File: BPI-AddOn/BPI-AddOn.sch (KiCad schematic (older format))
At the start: 61 parts, among them CON1 BARREL_JACK, J1 RJ45, J2 RJ45, J3 RJ45, P1 DIN10-1, P10 CONN_01X03, P11 CONN_01X05, P12 CONN_01X05, P13 CONN_01X08, P15 CONN_02X11, P16 USB_B, P17 CONN_01X05, P18 CONN_01X05, P19 V, P2 DIN10-2, P20 - +, P21 USB_OTG, P22 CONN_01X06, P23 CONN_01X06, P24 CONN_02X02, P25 CONN_01X02, P3 DIN10-3, P4 DIN10-4, P5 DIN10-5, P6 DIN7-1, P7 DIN7-2, P8 DIN7-3, P9 CONN_01X03, U1 MC34063, U2 FT230XS

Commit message: routing ...
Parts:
- R3: footprint w_pth_resistors:RC03 -> w_pth_resistors:RC05
- renumbered F3 to Fe1
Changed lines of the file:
@@
 $EndComp
 $Comp
-L R F3
+L R Fe1
 U 1 1 576471B3
 P 7450 4400
-F 0 "F3" V 7530 4400 50  0000 C CNN
+F 0 "Fe1" V 7530 4400 50  0000 C CNN
 F 1 "Ferrit" V 7450 4400 50  0000 C CNN
 F 2 "Resistors_SMD:R_0805_HandSoldering" V 7380 4400 50  0001 C CNN
@@
 F 0 "R3" V 2280 4450 50  0000 C CNN
 F 1 "120" V 2200 4450 50  0000 C CNN
-F 2 "w_pth_resistors:RC03" V 2130 4450 50  0001 C CNN
+F 2 "w_pth_resistors:RC05" V 2130 4450 50  0001 C CNN
 F 3 "" H 2200 4450 50  0000 C CNN
 	1    2200 4450

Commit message: wip
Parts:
- C5: value 10nF -> 100nF
- C8: value 10nF -> 4.7uF
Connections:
- wire segments 308 -> 305
- no-connect marks 23 -> 28
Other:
- moved on the sheet: C5, C9, CON1
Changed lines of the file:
@@
 	3700 5750 3800 5650
 Entry Wire Line
-	3800 5750 3900 5650
-Entry Wire Line
 	3900 5750 4000 5650
 Entry Wire Line
-	4000 5750 4100 5650
-Entry Wire Line
 	4100 5750 4200 5650
 Entry Wire Line
@@
 	4750 5750 4850 5650
 Entry Wire Line
-	4850 5750 4950 5650
-Entry Wire Line
 	4950 5750 5050 5650
-Entry Wire Line
-	5050 5750 5150 5650
 Entry Wire Line
 	5150 5750 5250 5650
@@
 CANL
 Text Label 4000 5550 1    60   ~ 0
-GND
-Text Label 3900 5550 1    60   ~ 0
-GND
-Text Label 4950 5550 1    60   ~ 0
 GND
 Text Label 5050 5550 1    60   ~ 0
@@
 Text Label 4750 5550 1    60   ~ 0
 GSB
-Text Label 4100 5550 1    60   ~ 0
-J1_V
 Text Label 4200 5550 1    60   ~ 0
 J1_V
-Text Label 5150 5550 1    60   ~ 0
-J2_V
 Text Label 5250 5550 1    60   ~ 0
 J2_V
@@
 L BARREL_JACK CON1
 U 1 1 575B93EA
-P 1550 6400
-F 0 "CON1" H 1550 6650 50  0000 C CNN
-F 1 "BARREL_JACK" H 1550 6200 50  0000 C CNN
-F 2 "w_conn_misc:dc_socket" H 1550 6400 50  0001 C CNN
-F 3 "" H 1550 6400 50  0000 C CNN
-	1    1550 6400
+P 1550 6450
+F 0 "CON1" H 1550 6700 50  0000 C CNN
+F 1 "BARREL_JACK" H 1550 6250 50  0000 C CNN
+F 2 "w_conn_misc:dc_socket" H 1550 6450 50  0001 C CNN
+F 3 "" H 1550 6450 50  0000 C CNN
+	1    1550 6450
 	1    0    0    -1
 $EndComp
@@
 L GNDA #PWR011
 U 1 1 575B9523
-P 2100 6600
-F 0 "#PWR011" H 2100 6350 50  0001 C CNN
-F 1 "GNDA" H 2100 6450 50  0000 C CNN
-F 2 "" H 2100 6600 50  0000 C CNN
-F 3 "" H 2100 6600 50  0000 C CNN
-	1    2100 6600
+P 2100 6650
+F 0 "#PWR011" H 2100 6400 50  0001 C CNN
+F 1 "GNDA" H 2100 6500 50  0000 C CNN
+F 2 "" H 2100 6650 50  0000 C CNN
+F 3 "" H 2100 6650 50  0000 C CNN
+	1    2100 6650
 	1    0    0    -1
 $EndComp
@@
 L C C9
 U 1 1 57645485
-P 8000 5900
-F 0 "C9" H 8025 6000 50  0000 L CNN
-F 1 "100nF" H 8025 5800 50  0000 L CNN
-F 2 "Resistors_SMD:R_0805_HandSoldering" H 8038 5750 50  0001 C CNN
-F 3 "" H 8000 5900 50  0000 C CNN
-	1    8000 5900
+P 7300 4750
+F 0 "C9" H 7325 4850 50  0000 L CNN
+F 1 "100nF" H 7325 4650 50  0000 L CNN
+F 2 "Resistors_SMD:R_0805_HandSoldering" H 7338 4600 50  0001 C CNN
+F 3 "" H 7300 4750 50  0000 C CNN
+	1    7300 4750
 	1    0    0    -1
 $EndComp
@@
 L C C5
 U 1 1 57653A31
-P 7300 4750
-F 0 "C5" H 7325 4850 50  0000 L CNN
-F 1 "10nF" H 7325 4650 50  0000 L CNN
-F 2 "Resistors_SMD:R_0805_HandSoldering" H 7338 4600 50  0001 C CNN
-F 3 "" H 7300 4750 50  0000 C CNN
-	1    7300 4750
+P 8000 5900
+F 0 "C5" H 8025 6000 50  0000 L CNN
+F 1 "100nF" H 8025 5800 50  0000 L CNN
+F 2 "Resistors_SMD:R_0805_HandSoldering" H 8038 5750 50  0001 C CNN
+F 3 "" H 8000 5900 50  0000 C CNN
+	1    8000 5900
 	1    0    0    -1
 $EndComp
@@
 P 7600 4750
 F 0 "C8" H 7625 4850 50  0000 L CNN
-F 1 "10nF" H 7625 4650 50  0000 L CNN
+F 1 "4.7uF" H 7625 4650 50  0000 L CNN
 F 2 "Resistors_SMD:R_0805_HandSoldering" H 7638 4600 50  0001 C CNN
 F 3 "" H 7600 4750 50  0000 C CNN
@@
 	3800 5300 3800 5650
 Wire Wire Line
-	3900 5300 3900 5650
-Wire Wire Line
 	4000 5300 4000 5650
 Wire Wire Line
-	4100 5300 4100 5650
-Wire Wire Line
 	4200 5300 4200 5650
 Wire Wire Line
@@
 	4850 5300 4850 5650
 Wire Wire Line
-	4950 5300 4950 5650
-Wire Wire Line
 	5050 5300 5050 5650
-Wire Wire Line
-	5150 5300 5150 5650
 Wire Wire Line
 	5250 5300 5250 5650
@@
 	2000 6900 1900 6900
 Wire Wire Line
-	1850 6300 2100 6300
-Wire Wire Line
-	2100 6300 2100 6600
-Wire Wire Line
-	1850 6400 2100 6400
-Connection ~ 2100 6400
-Wire Wire Line
-	1850 6500 2400 6500
+	1850 6350 2100 6350
+Wire Wire Line
+	2100 6350 2100 6650
 Wire Wire Line
 	2400 7100 2300 7100
@@
 	7350 5650 7350 5350
 Connection ~ 7350 5350
-Wire Wire Line
-	6550 6000 7550 6000
 Connection ~ 7350 6000
 Wire Wire Line
@@
 Wire Wire Line
 	7550 6000 7550 5950
-Wire Wire Line
-	6550 6000 6550 5850
-Connection ~ 6950 6000
 Wire Wire Line
 	10150 5050 10150 5150
@@
 	1800 4950 2050 4950
 Wire Wire Line
-	2050 4850 2050 4600
+	2050 4600 2050 4850
 Wire Wire Line
 	2050 4650 2200 4650
@@
 Connection ~ 2050 4650
 Wire Wire Line
-	2200 4300 2200 4200
-Wire Wire Line
-	2200 4200 1800 4200
+	2200 4200 2200 4300
+Wire Wire Line
+	1800 4200 2200 4200
 Wire Wire Line
 	2050 4300 2050 4200
@@
 Text Label 4900 7350 1    60   ~ 0
 GNDB
+NoConn ~ 4100 5300
+NoConn ~ 3900 5300
+NoConn ~ 5150 5300
+NoConn ~ 4950 5300
+Wire Wire Line
+	1850 6450 2300 6450
+Wire Wire Line
+	2300 6450 2300 6500
+Wire Wire Line
+	2300 6500 2400 6500
+Wire Wire Line
+	1850 6550 2100 6550
+Connection ~ 2100 6550
+Wire Wire Line
+	6950 6000 7550 6000
+NoConn ~ 6550 5850
 $EndSCHEMATC

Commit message: wip
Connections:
- net labels removed: GND
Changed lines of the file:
@@
 Vcc
 Text Label 850  2600 0    60   ~ 0
-GND
+GNDA
 Text Label 850  3000 0    60   ~ 0
-GND
+GNDA
 Text Label 1800 2600 0    60   ~ 0
-GND
+GNDA
 Text Label 1800 3000 0    60   ~ 0
-GND
+GNDA
 Text Label 850  4250 0    60   ~ 0
-GND
+GNDA
 Text Label 850  4650 0    60   ~ 0
-GND
+GNDA
 Text Label 2750 900  0    60   ~ 0
-GND
+GNDA
 Text Label 2750 2600 0    60   ~ 0
-GND
+GNDA
 Text Label 2750 1300 0    60   ~ 0
-GND
+GNDA
 Text Label 2750 3000 0    60   ~ 0
-GND
+GNDA
 Text Label 2750 800  0    60   ~ 0
 Vcc
@@
 GS0
 Text Label 850  900  0    60   ~ 0
-GND
+GNDA
 Text Label 850  1300 0    60   ~ 0
-GND
+GNDA
 Text Label 1800 1300 0    60   ~ 0
-GND
+GNDA
 Text Label 1800 900  0    60   ~ 0
-GND
+GNDA
 Text Label 2750 2900 0    60   ~ 0
 GS0
@@
 CANL
 Text Label 4000 5550 1    60   ~ 0
-GND
+GNDA
 Text Label 5050 5550 1    60   ~ 0
-GND
+GNDA
 $Comp
 L CONN_01X03 P9
@@
 5V
 Text Label 3500 2400 0    60   ~ 0
-GND
+GNDA
 $Comp
 L CONN_01X05 P11
@@
 5V
 Text Label 3500 3200 0    60   ~ 0
-GND
+GNDA
 Text Label 3500 3100 0    60   ~ 0
 Vcc
@@
 Vcc
 Text Label 4400 3200 0    60   ~ 0
-GND
+GNDA
 Text Label 4400 3300 0    60   ~ 0
 5V
@@
 Vcc
 Text Label 4400 2400 0    60   ~ 0
-GND
+GNDA
 Text Label 4400 2500 0    60   ~ 0
 5V
@@
 CANH
 Text Label 2750 4250 0    60   ~ 0
-GND
+GNDA
 Text Label 2750 4650 0    60   ~ 0
-GND
+GNDA
 Text Label 2750 4150 0    60   ~ 0
 Vcc

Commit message: wip
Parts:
- added P14: CONN_02X11, Pin_Headers:Pin_Header_Straight_2x11, symbol CONN_02X11
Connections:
- net labels added: 21_01, 21_02, 21_03, 21_04, 21_05, 21_06, 21_07, 21_08, 21_09, 21_10, 21_11, 21_12, 21_13, 21_14, 21_15, 21_16, 21_17, 21_18, 21_19, 21_20, 21_21, VAA
- net labels removed: VCC
- wire segments 305 -> 342
- no-connect marks 28 -> 14

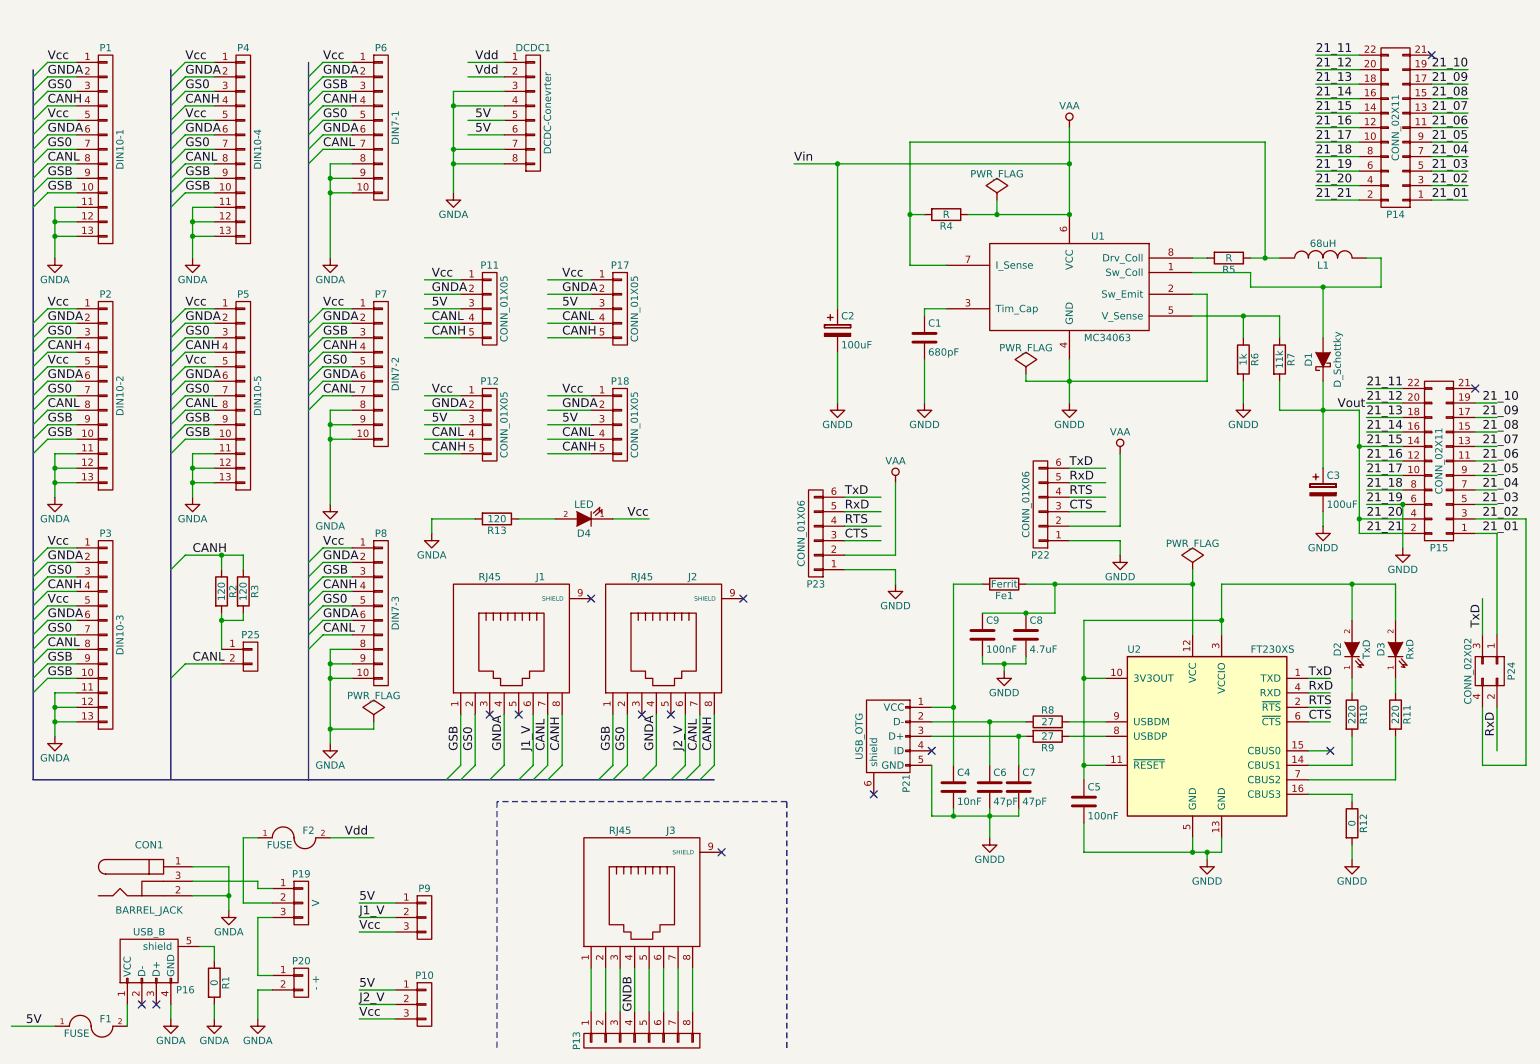
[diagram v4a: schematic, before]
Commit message: add LED for GLeisbox
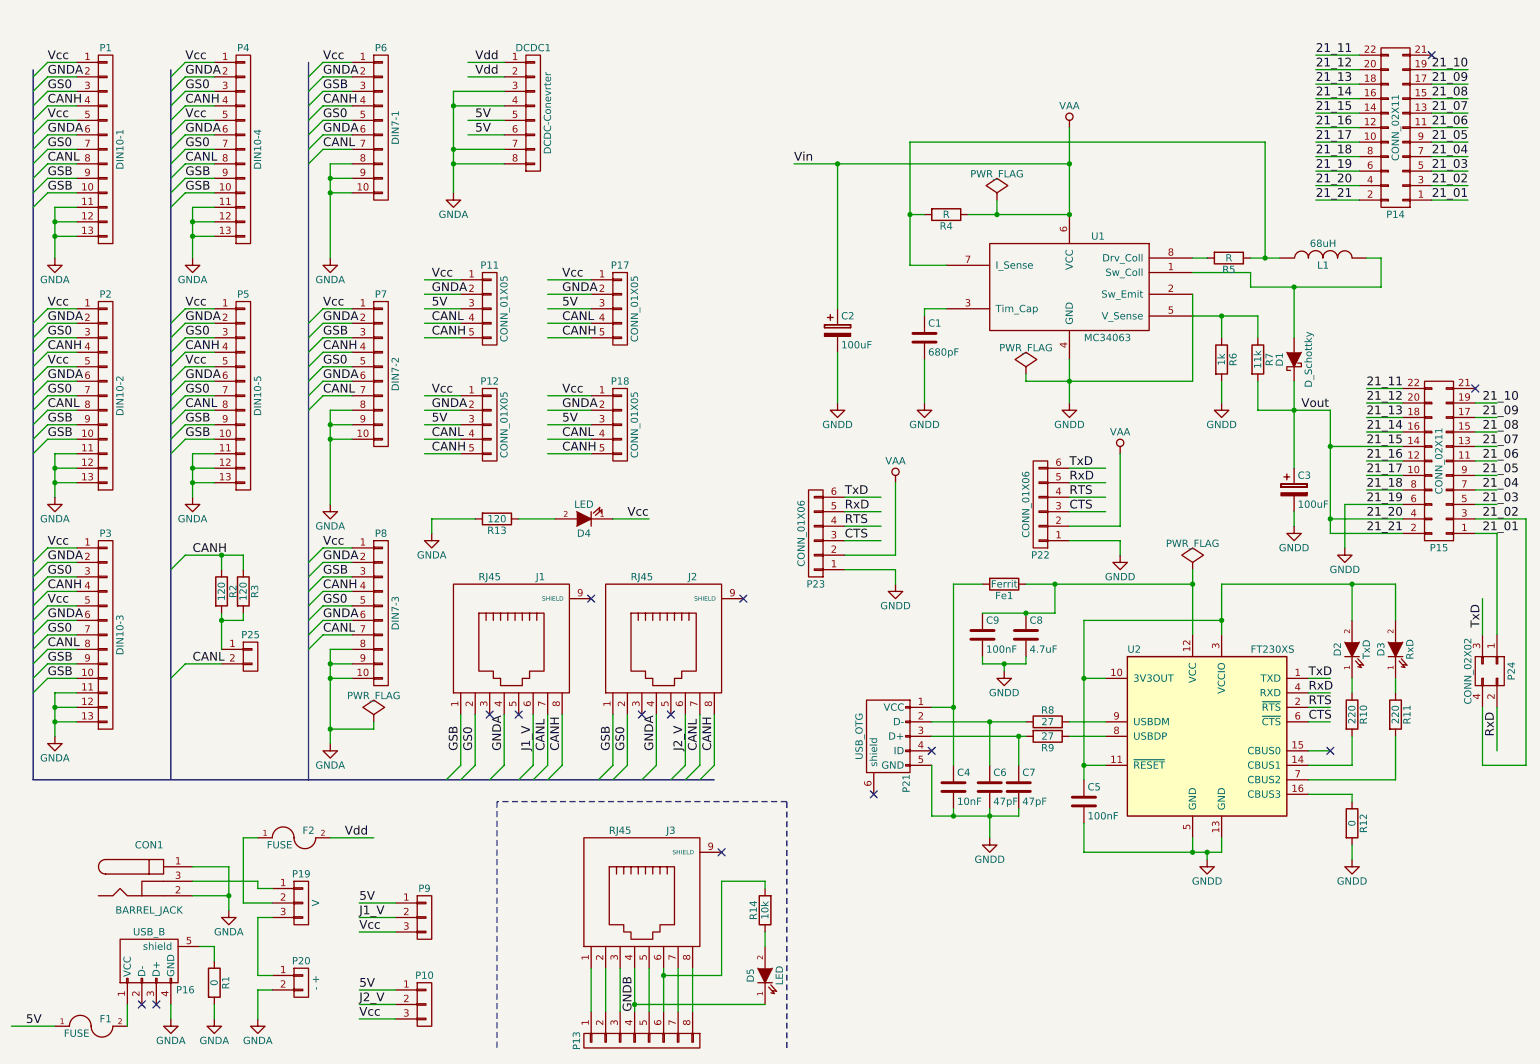
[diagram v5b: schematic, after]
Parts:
- added D5: LED, LEDs:LED-5MM, symbol LED
- added R14: 10k, w_pth_resistors:RC05, symbol R
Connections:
- wire segments 342 -> 348
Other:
- moved on the sheet: C3, D1, R6, R7
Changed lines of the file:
@@
 L R R6
 U 1 1 575ADF4D
-P 9100 2850
-F 0 "R6" V 9180 2850 50  0000 C CNN
-F 1 "1k" V 9100 2850 50  0000 C CNN
-F 2 "w_pth_resistors:RC03" V 9030 2850 50  0001 C CNN
-F 3 "" H 9100 2850 50  0000 C CNN
-	1    9100 2850
+P 8950 2850
+F 0 "R6" V 9030 2850 50  0000 C CNN
+F 1 "1k" V 8950 2850 50  0000 C CNN
+F 2 "w_pth_resistors:RC03" V 8880 2850 50  0001 C CNN
+F 3 "" H 8950 2850 50  0000 C CNN
+	1    8950 2850
 	1    0    0    -1
 $EndComp
@@
 L R R7
 U 1 1 575AE02D
-P 9350 2850
-F 0 "R7" V 9430 2850 50  0000 C CNN
-F 1 "11k" V 9350 2850 50  0000 C CNN
-F 2 "w_pth_resistors:RC03" V 9280 2850 50  0001 C CNN
-F 3 "" H 9350 2850 50  0000 C CNN
-	1    9350 2850
+P 9200 2850
+F 0 "R7" V 9280 2850 50  0000 C CNN
+F 1 "11k" V 9200 2850 50  0000 C CNN
+F 2 "w_pth_resistors:RC03" V 9130 2850 50  0001 C CNN
+F 3 "" H 9200 2850 50  0000 C CNN
+	1    9200 2850
 	1    0    0    -1
 $EndComp
@@
 L GNDD #PWR017
 U 1 1 575AE0AF
-P 9100 3150
-F 0 "#PWR017" H 9100 2900 50  0001 C CNN
-F 1 "GNDD" H 9100 3000 50  0000 C CNN
-F 2 "" H 9100 3150 50  0000 C CNN
-F 3 "" H 9100 3150 50  0000 C CNN
-	1    9100 3150
+P 8950 3150
+F 0 "#PWR017" H 8950 2900 50  0001 C CNN
+F 1 "GNDD" H 8950 3000 50  0000 C CNN
+F 2 "" H 8950 3150 50  0000 C CNN
+F 3 "" H 8950 3150 50  0000 C CNN
+	1    8950 3150
 	1    0    0    -1
 $EndComp
@@
 L D_Schottky D1
 U 1 1 575AE51D
-P 9650 2850
-F 0 "D1" H 9650 2950 50  0000 C CNN
-F 1 "D_Schottky" H 9650 2750 50  0000 C CNN
-F 2 "Diodes_ThroughHole:Diode_DO-35_SOD27_Horizontal_RM10" H 9650 2850 50  0001 C CNN
-F 3 "" H 9650 2850 50  0000 C CNN
-	1    9650 2850
+P 9450 2850
+F 0 "D1" H 9450 2950 50  0000 C CNN
+F 1 "D_Schottky" H 9450 2750 50  0000 C CNN
+F 2 "Diodes_ThroughHole:Diode_DO-35_SOD27_Horizontal_RM10" H 9450 2850 50  0001 C CNN
+F 3 "" H 9450 2850 50  0000 C CNN
+	1    9450 2850
 	0    -1   -1   0
 $EndComp
@@
 L CP C3
 U 1 1 575AF2D7
-P 9650 3750
-F 0 "C3" H 9675 3850 50  0000 L CNN
-F 1 "100uF" H 9675 3650 50  0000 L CNN
-F 2 "w_capacitors:CP_5x11mm" H 9688 3600 50  0001 C CNN
-F 3 "" H 9650 3750 50  0000 C CNN
-	1    9650 3750
+P 9450 3750
+F 0 "C3" H 9475 3850 50  0000 L CNN
+F 1 "100uF" H 9475 3650 50  0000 L CNN
+F 2 "w_capacitors:CP_5x11mm" H 9488 3600 50  0001 C CNN
+F 3 "" H 9450 3750 50  0000 C CNN
+	1    9450 3750
 	1    0    0    -1
 $EndComp
@@
 L GNDD #PWR018
 U 1 1 575AF39C
-P 9650 4000
-F 0 "#PWR018" H 9650 3750 50  0001 C CNN
-F 1 "GNDD" H 9650 3850 50  0000 C CNN
-F 2 "" H 9650 4000 50  0000 C CNN
-F 3 "" H 9650 4000 50  0000 C CNN
-	1    9650 4000
-	1    0    0    -1
-$EndComp
-Text Label 9750 3200 0    60   ~ 0
+P 9450 4000
+F 0 "#PWR018" H 9450 3750 50  0001 C CNN
+F 1 "GNDD" H 9450 3850 50  0000 C CNN
+F 2 "" H 9450 4000 50  0000 C CNN
+F 3 "" H 9450 4000 50  0000 C CNN
+	1    9450 4000
+	1    0    0    -1
+$EndComp
+Text Label 9500 3200 0    60   ~ 0
 Vout
 $Comp
@@
 L GNDD #PWR029
 U 1 1 57660AB6
-P 10200 4150
-F 0 "#PWR029" H 10200 3900 50  0001 C CNN
-F 1 "GNDD" H 10200 4000 50  0000 C CNN
-F 2 "" H 10200 4150 50  0000 C CNN
-F 3 "" H 10200 4150 50  0000 C CNN
-	1    10200 4150
+P 9800 4150
+F 0 "#PWR029" H 9800 3900 50  0001 C CNN
+F 1 "GNDD" H 9800 4000 50  0000 C CNN
+F 2 "" H 9800 4150 50  0000 C CNN
+F 3 "" H 9800 4150 50  0000 C CNN
+	1    9800 4150
 	1    0    0    -1
 $EndComp
@@
 	7400 1850 7400 1750
 Wire Wire Line
-	7600 3000 8850 3000
+	7600 3000 8750 3000
 Wire Wire Line
 	7600 3000 7600 2950
@@
 Connection ~ 7900 1850
 Wire Wire Line
-	8750 2400 8850 2400
-Wire Wire Line
-	8850 2400 8850 3000
+	8750 2400 8750 2400
+Wire Wire Line
+	8750 3000 8750 2400
 Wire Wire Line
 	6800 2200 7050 2200
@@
 	9150 2250 8750 2250
 Wire Wire Line
-	9100 2700 9100 2550
-Wire Wire Line
-	8750 2550 9350 2550
-Wire Wire Line
-	9100 3000 9100 3150
-Wire Wire Line
-	9350 2550 9350 2700
-Connection ~ 9100 2550
-Wire Wire Line
-	9350 3000 9350 3200
-Wire Wire Line
-	9350 3200 9900 3200
-Wire Wire Line
-	9650 3000 9650 3600
-Wire Wire Line
-	9650 2700 9650 2350
-Connection ~ 9650 2350
-Connection ~ 9650 3200
-Wire Wire Line
-	9650 3900 9650 4000
+	8950 2700 8950 2550
+Wire Wire Line
+	8750 2550 9200 2550
+Wire Wire Line
+	8950 3000 8950 3150
+Wire Wire Line
+	9200 2550 9200 2700
+Connection ~ 8950 2550
+Wire Wire Line
+	9200 3000 9200 3200
+Wire Wire Line
+	9200 3200 9700 3200
+Wire Wire Line
+	9450 3000 9450 3600
+Wire Wire Line
+	9450 2700 9450 2350
+Connection ~ 9450 2350
+Connection ~ 9450 3200
+Wire Wire Line
+	9450 3900 9450 4000
 Wire Wire Line
 	6300 2800 6300 3150
@@
 	10750 4750 10750 4500
 Wire Wire Line
-	10200 3450 9900 3450
-Wire Wire Line
-	9900 3200 9900 4050
-Wire Wire Line
-	9900 4050 10200 4050
-Wire Wire Line
-	10200 3950 9900 3950
-Connection ~ 9900 3950
-Connection ~ 9900 3450
-Wire Wire Line
-	10200 3850 10200 4150
+	10200 3450 9700 3450
+Wire Wire Line
+	9700 3200 9700 4050
+Wire Wire Line
+	9700 4050 10200 4050
+Wire Wire Line
+	10200 3950 9700 3950
+Connection ~ 9700 3950
+Connection ~ 9700 3450
 Wire Wire Line
 	1800 4950 2050 4950
@@
 	9950 3750 10200 3750
 Wire Wire Line
-	9950 3850 10200 3850
+	9800 3850 10200 3850
 Wire Wire Line
 	10850 3850 10700 3850
@@
 Wire Wire Line
 	10850 3150 10700 3150
-Connection ~ 10200 3850
 Wire Wire Line
 	10650 850  10400 850
@@
 Text Label 9600 1750 0    60   ~ 0
 21_21
+Wire Wire Line
+	9800 3850 9800 4150
+$Comp
+L LED D5
+U 1 1 576A6C99
+P 5800 7100
+F 0 "D5" H 5800 7200 50  0000 C CNN
+F 1 "LED" H 5800 7000 50  0000 C CNN
+F 2 "LEDs:LED-5MM" H 5800 7100 50  0001 C CNN
+F 3 "" H 5800 7100 50  0000 C CNN
+	1    5800 7100
+	0    -1   -1   0
+$EndComp
+$Comp
+L R R14
+U 1 1 576A6F10
+P 5800 6650
+F 0 "R14" V 5880 6650 50  0000 C CNN
+F 1 "10k" V 5800 6650 50  0000 C CNN
+F 2 "w_pth_resistors:RC05" V 5730 6650 50  0001 C CNN
+F 3 "" H 5800 6650 50  0000 C CNN
+	1    5800 6650
+	-1   0    0    1
+$EndComp
+Wire Wire Line
+	5800 7300 4900 7300
+Connection ~ 4900 7300
+Wire Wire Line
+	5800 6900 5800 6800
+Wire Wire Line
+	5800 6500 5800 6450
+Wire Wire Line
+	5800 6450 5500 6450
+Wire Wire Line
+	5500 6450 5500 7100
+Wire Wire Line
+	5500 7100 5100 7100
+Connection ~ 5100 7100
 $EndSCHEMATC

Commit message: wip
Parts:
- added P26, P28: CONN_01X03, Pin_Headers:Pin_Header_Straight_1x03, symbol CONN_01X03
- added P27: CONN_01X04, Pin_Headers:Pin_Header_Straight_1x04, symbol CONN_01X04
- added Q1, Q2, Q3, Q4: BS170, w_to:to92_3_flat, symbol BS170
- added R15, R16, R17, R18, R19, R20, R21, R22: 4k7, w_pth_resistors:RC03, symbol R
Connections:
- net labels added: Vccio, Vusb, _CTS, _RTS, _RxD, _TxD
- wire segments 348 -> 401
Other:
- moved on the sheet: C1, C2, C3, D1, L1, P14, P23, R4, R5, R6, R7
